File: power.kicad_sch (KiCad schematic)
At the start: 41 parts, among them T1 net-tie, U2 TPS546D24ARVFR

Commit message: All components placed
Went through TI schematic and layout checklist.
All components placed and initial DRC
Need thermal vias on KF1950 and also better layout (so not so many errors)
Need to do silk
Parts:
- added Q4: MMBT2222A, Package_TO_SOT_SMD:SOT-23, symbol Transistor_BJT:MMBT2222A
- added R18: 100, Resistor_SMD:R_0402_1005Metric, symbol Device:R_US
- added R20: 0, Resistor_SMD:R_1206_3216Metric, symbol Device:R_US
- R1: value 8.25k -> 4.64k
- R10: value 68.1k -> 0
- R5: value 14.7k -> 4.64k
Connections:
- net AGND: now also Q4.2 (E)
- net at C8.1, R8.1, R9.2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: now also Q4.3 (C)
- net at C12.1: now also R20.1; no longer U2.7 (BOOT)
- new net: Q4.1 (B), R18.2
- new net: R20.2, U2.7 (BOOT)
- new net /TPS_EN: R18.1
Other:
- note added: "Need to keep TPS off until the PMBus has configured it for 0.3V."
- note added: "The resistor dividers follow the TPS546 spreadsheet except the address which follows Bitaxe Gamma"
- moved on the sheet: C12, C5, C8, R11, R9

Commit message: Silk Done
Still need to fix up heatsink vias on ASIC and paste layer for thermal
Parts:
- C12: footprint Capacitor_SMD:C_0402_1005Metric -> Capacitor_SMD:C_0603_1608Metric
- R20: footprint Resistor_SMD:R_1206_3216Metric -> Resistor_SMD:R_0402_1005Metric
- renumbered TP4 to GND, TP3 to VDD
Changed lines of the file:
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@@
 	(wire
 		(pts
+			(xy 49.53 17.78) (xy 59.69 17.78)
+		)
+		(stroke
+			(width 0)
+			(type default)
+		)
+	)
+	(wire
+		(pts
 			(xy 234.95 43.18) (xy 234.95 57.15)
 		)
@@
 	(wire
 		(pts
+			(xy 59.69 34.29) (xy 69.85 34.29)
+		)
+		(stroke
+			(width 0)
+			(type default)
+		)
+	)
+	(wire
+		(pts
 			(xy 181.61 39.37) (xy 189.23 39.37)
 		)
@@
 	(wire
 		(pts
-			(xy 49.53 17.78) (xy 59.69 17.78)
-		)
-		(stroke
-			(width 0)
-			(type default)
-		)
-	)
-	(wire
-		(pts
 			(xy 78.74 46.99) (xy 92.71 46.99)
 		)
@@
 	(wire
 		(pts
-			(xy 59.69 34.29) (xy 69.85 34.29)
-		)
-		(stroke
-			(width 0)
-			(type default)
-		)
-	)
-	(wire
-		(pts
 			(xy 227.33 39.37) (xy 234.95 39.37)
 		)
@@
 		(on_board yes)
 		(dnp no)
-		(property "Reference" "TP4"
+		(property "Reference" "GND"
 			(at 241.3 86.36 90)
 			(effects
@@
 			(project "bitaxeGamma"
 				(path "/e63e39d7-6ac0-4ffd-8aa3-1841a4541b55/8ec0a9c6-2b78-44ef-a83d-9047d2828409"
-					(reference "TP4")
+					(reference "GND")
 					(unit 1)
 				)
@@
 		(on_board yes)
 		(dnp no)
-		(property "Reference" "TP3"
+		(property "Reference" "VDD"
 			(at 241.3 43.18 90)
 			(effects
@@
 			(project "bitaxeGamma"
 				(path "/e63e39d7-6ac0-4ffd-8aa3-1841a4541b55/8ec0a9c6-2b78-44ef-a83d-9047d2828409"
-					(reference "TP3")
+					(reference "VDD")
 					(unit 1)
 				)
@@
 			)
 		)
-		(property "Footprint" "Resistor_SMD:R_1206_3216Metric"
+		(property "Footprint" "Resistor_SMD:R_0402_1005Metric"
 			(at 140.716 36.576 90)
 			(effects
@@
 			)
 		)
-		(property "Footprint" "Capacitor_SMD:C_0402_1005Metric"
+		(property "Footprint" "Capacitor_SMD:C_0603_1608Metric"
 			(at 153.67 34.5948 0)
 			(effects

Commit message: PCB fixes
Fixed up KF1950 footprint
Added heatsinking to the bottom
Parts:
- renumbered GND to GND1, VDD to VDD1
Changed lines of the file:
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@@
 		(on_board yes)
 		(dnp no)
-		(property "Reference" "GND"
+		(property "Reference" "GND1"
 			(at 241.3 86.36 90)
 			(effects
@@
 			(project "bitaxeGamma"
 				(path "/e63e39d7-6ac0-4ffd-8aa3-1841a4541b55/8ec0a9c6-2b78-44ef-a83d-9047d2828409"
-					(reference "GND")
+					(reference "GND1")
 					(unit 1)
 				)
@@
 		(on_board yes)
 		(dnp no)
-		(property "Reference" "VDD"
+		(property "Reference" "VDD1"
 			(at 241.3 43.18 90)
 			(effects
@@
 			(project "bitaxeGamma"
 				(path "/e63e39d7-6ac0-4ffd-8aa3-1841a4541b55/8ec0a9c6-2b78-44ef-a83d-9047d2828409"
-					(reference "VDD")
-					(unit 1)
-				)
+					(reference "VDD1")
+					(unit 1)
+				)

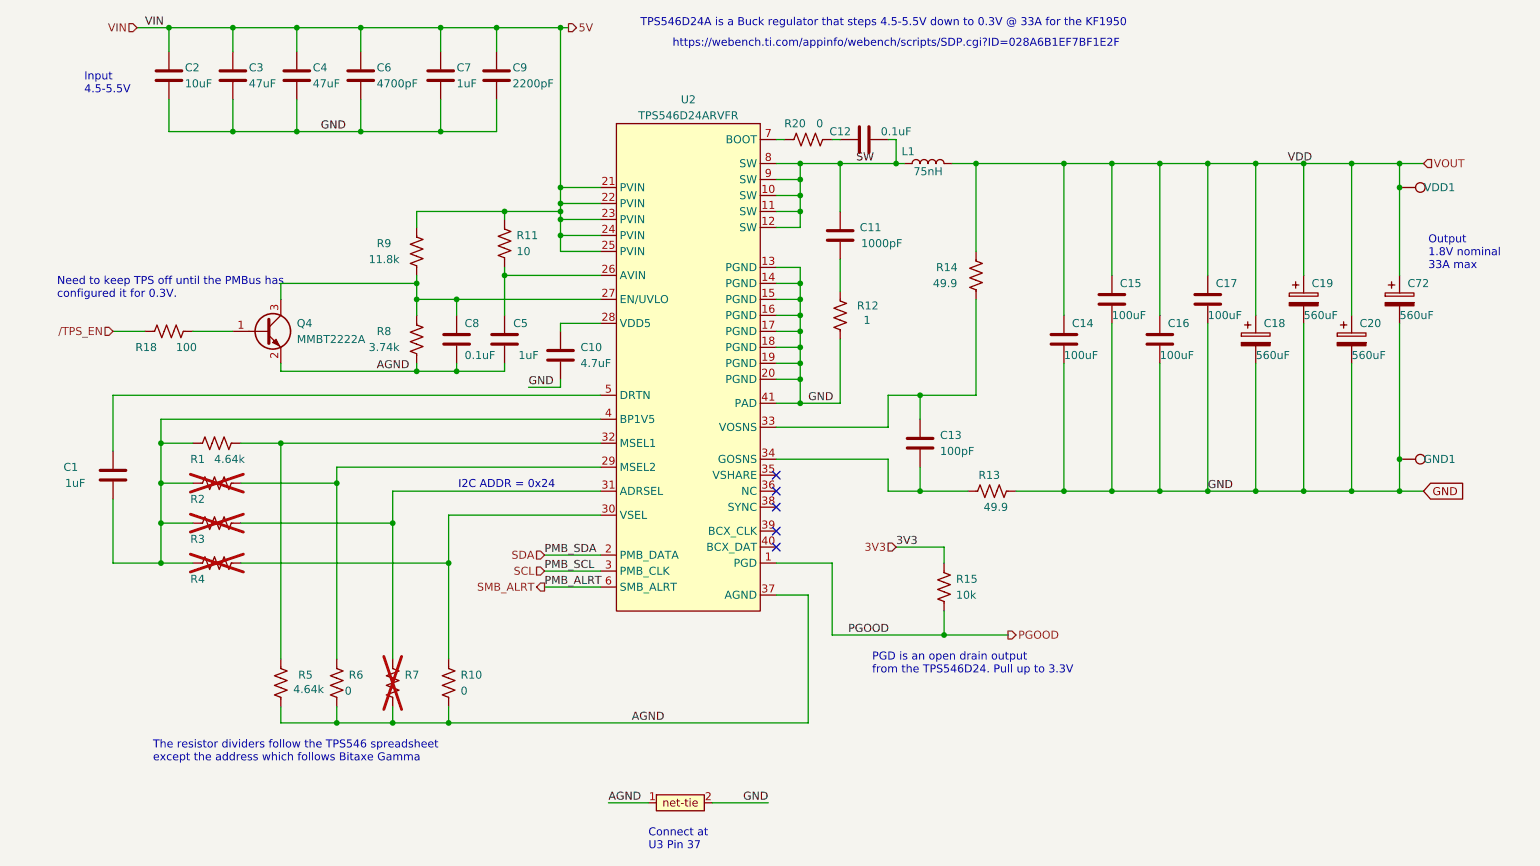
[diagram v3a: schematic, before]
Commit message: Manfacturing prep
Add part numbers and did initial BOM optimization (Hope to do more after testing)
Created Manufacturing files
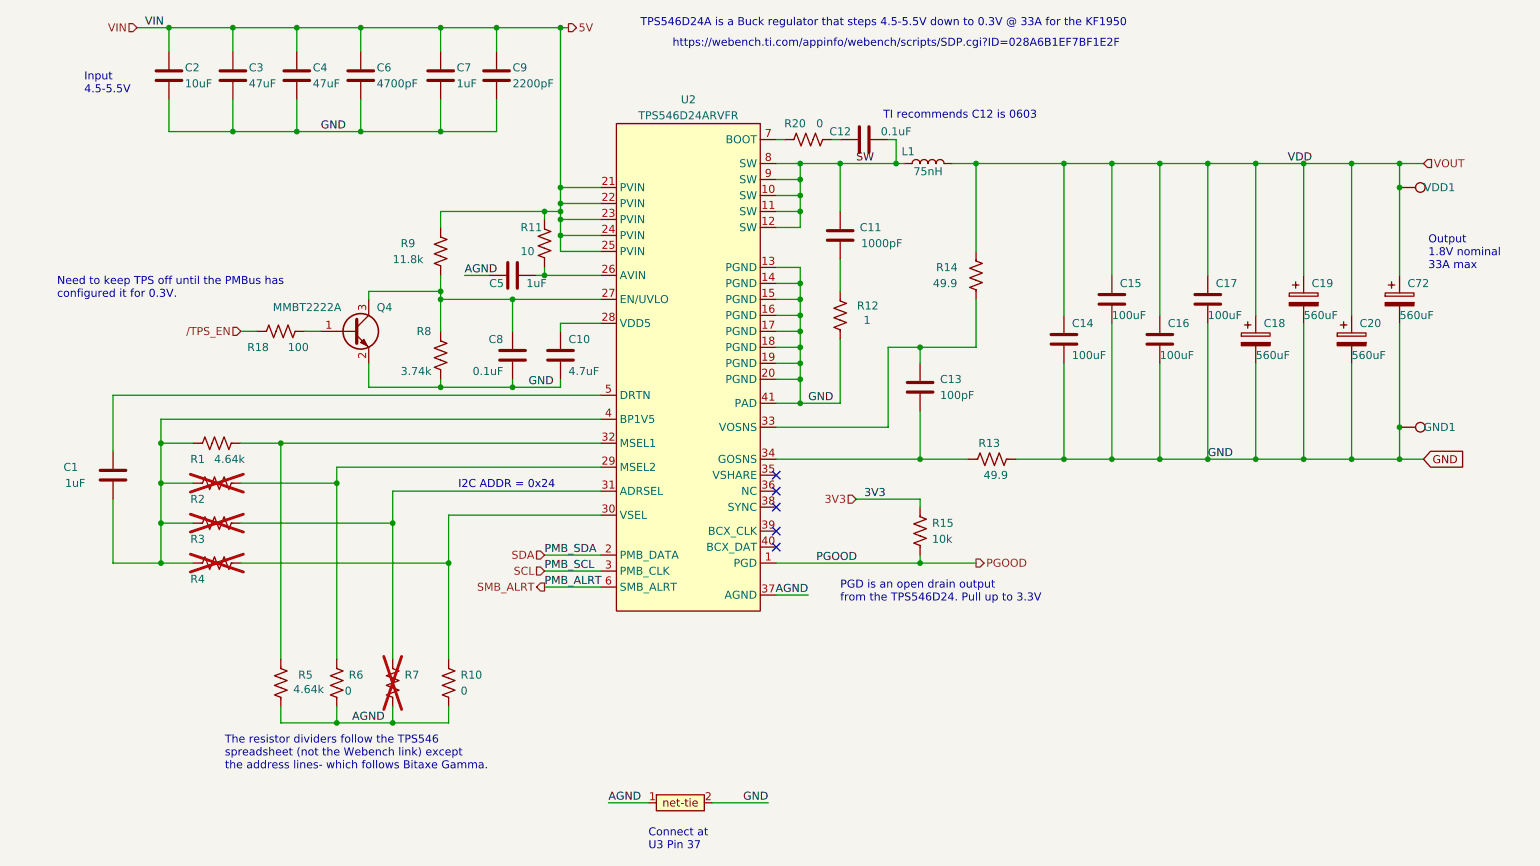
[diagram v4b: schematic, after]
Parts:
- C14: footprint Capacitor_SMD:C_1210_3225Metric -> Capacitor_SMD:C_1206_3216Metric
- C15, C16, C17: footprint Capacitor_SMD:C_1210_3225Metric -> Capacitor_SMD:C_1206_3216Metric; PARTNO GRM32EC80J107ME20L -> (none)
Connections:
- net AGND: now also C5.2; no longer C5.1, C8.2, Q4.2 (E), R8.2
- net GND: now also C8.2, Q4.2 (E), R8.2
- net at R11.2, U2.26 (AVIN): now also C5.1; no longer C5.2
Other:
- note added: "TI recommends C12 is 0603"
- note added: "The resistor dividers follow the TPS546 spreadsheet (not the Webench link) except the address lines- which follows Bitaxe Gamma."
- note removed: "The resistor dividers follow the TPS546 spreadsheet except the address which follows Bitaxe Gamma"
- moved on the sheet: C13, C5, C8, GND1, Q4, R11, R13, R15, R18, R8, R9

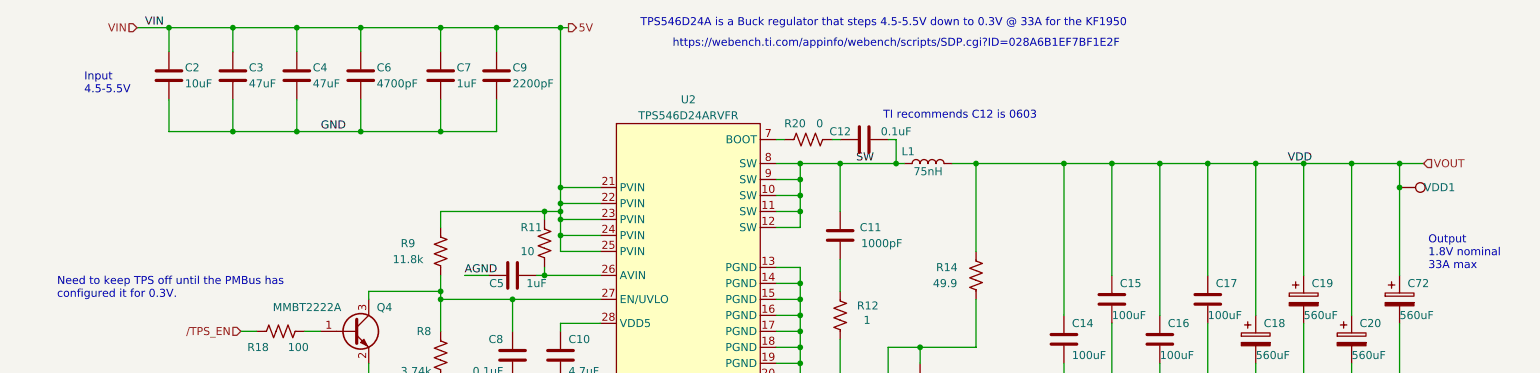
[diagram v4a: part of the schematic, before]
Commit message: Addressed Bitaxe Gamma Issues
- moved Fan caps
- added USB CC1 & CC2 pulldowns
- (I2C pullups were already done)
- reviewed but so far did not address any of the other issues/bugs
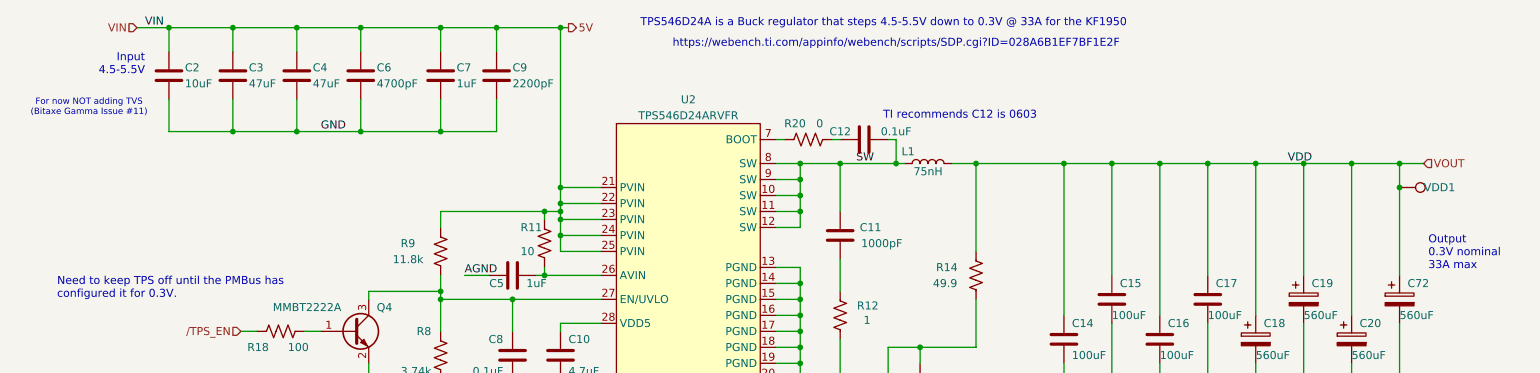
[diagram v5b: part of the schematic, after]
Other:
- note added: "For now NOT adding TVS (Bitaxe Gamma Issue #11)"
- note added: "Output 0.3V nominal 33A max"
- note removed: "Output 1.8V nominal 33A max"
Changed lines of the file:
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@@
 	(text "Input \n4.5-5.5V"
 		(exclude_from_sim no)
-		(at 25.908 28.448 0)
+		(at 35.56 25.4 0)
 		(effects
 			(font
 				(size 1.27 1.27)
 			)
-			(justify left bottom)
+			(justify right bottom)
 		)
 	)
@@
 		)
 	)
+	(text "For now NOT adding TVS\n(Bitaxe Gamma Issue #11)"
+		(exclude_from_sim no)
+		(at 26.67 30.48 0)
+		(effects
+			(font
+				(size 1 1)
+			)
+		)
+	)
 	(text "I2C ADDR = 0x24"
 		(exclude_from_sim no)
@@
 		)
 	)
-	(text "Output \n1.8V nominal\n33A max"
+	(text "Output \n0.3V nominal\n33A max"
 		(exclude_from_sim no)
 		(at 239.522 56.388 0)

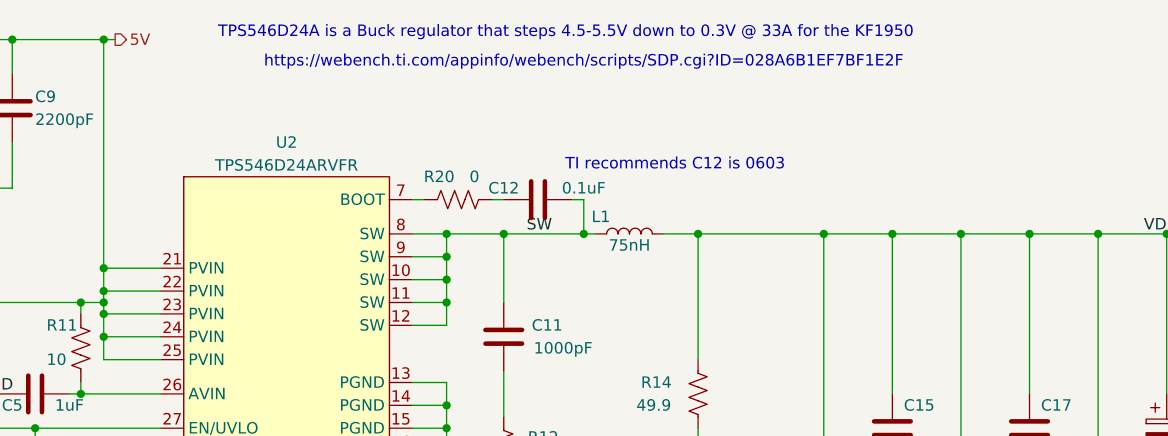
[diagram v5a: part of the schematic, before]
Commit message: New Inductor & BOM fix
Changed the inductor and cleaned up files for JLCPCB order.
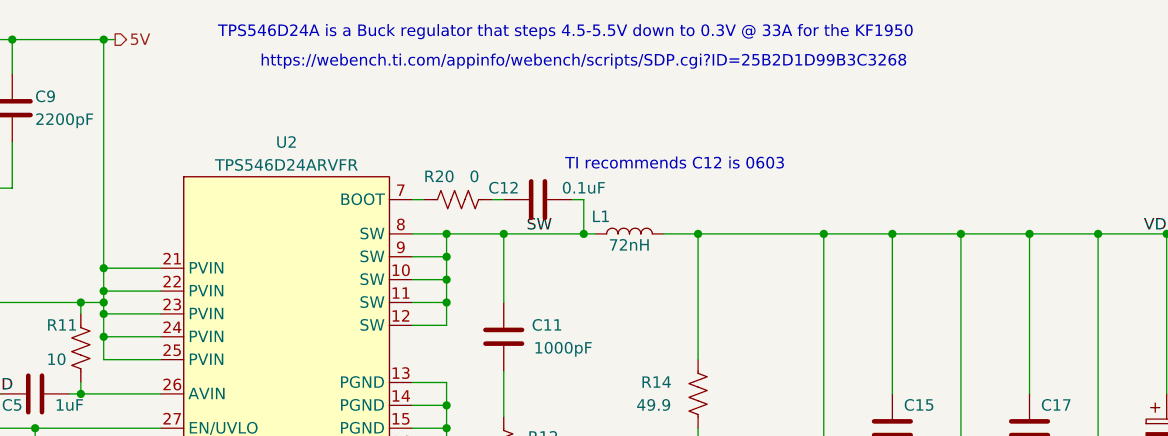
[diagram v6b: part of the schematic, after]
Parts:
- L1: value 75nH -> 72nH; footprint bitaxe:SLC1049 -> bitaxe:FP0805R1; PARTNO SLC1049-750MLB -> FP0805R1-R07-R
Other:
- note added: "https://webench.ti.com/appinfo/webench/scripts/SDP.cgi?ID=25B2D1D99B3C3268"
- note removed: "https://webench.ti.com/appinfo/webench/scripts/SDP.cgi?ID=028A6B1EF7BF1E2F"
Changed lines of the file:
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@@
 		)
 	)
-	(text "https://webench.ti.com/appinfo/webench/scripts/SDP.cgi?ID=028A6B1EF7BF1E2F"
+	(text "https://webench.ti.com/appinfo/webench/scripts/SDP.cgi?ID=25B2D1D99B3C3268"
 		(exclude_from_sim no)
 		(at 154.94 20.32 0)
@@
 			)
 		)
-		(property "Value" "75nH"
+		(property "Value" "72nH"
 			(at 160.02 40.64 90)
 			(effects
@@
 			)
 		)
-		(property "Footprint" "bitaxe:SLC1049"
+		(property "Footprint" "bitaxe:FP0805R1"
 			(at 160.02 39.37 0)
 			(effects
@@
 			)
 		)
-		(property "Datasheet" "https://www.coilcraft.com/getmedia/ef564b79-aee7-4fb3-aabd-a8bf1c568496/slc1049.pdf"
+		(property "Datasheet" "https://www.eaton.com/content/dam/eaton/products/electronic-components/resources/data-sheet/eaton-fp0805-power-inductor-data-sheet.pdf"
 			(at 160.02 39.37 0)
 			(effects
@@
 			)
 		)
-		(property "PARTNO" "SLC1049-750MLB"
+		(property "PARTNO" "FP0805R1-R07-R"
 			(at 160.02 39.37 90)
 			(effects
